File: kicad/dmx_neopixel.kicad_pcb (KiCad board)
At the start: 2 copper layers, 60.5 x 96.3 mm, 32 parts, among them J1 USB_C_Receptacle_USB2.0_16P, J7 Jack-DC

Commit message: feat: v0.2の基板を作成
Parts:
- removed the G*** at (148.1, 123.4)
- removed XH: Conn_01x03_Pin, Connector_JST:JST_XH_B3B-XH-A_1x03_P2.50mm_Vertical
- added ?: http://LDDG.ME/VLLD2N, QRCODE, B.Cu at (152.9, 117.3)
- added MODE: SW_Push, Button_Switch_SMD:SW_SPST_PTS810, B.Cu at (154.2, 56.6)
- added NEOPIXEL OUT: Conn_01x02_Pin, Connector_JST:JST_XH_B2B-XH-A_1x02_P2.50mm_Vertical, F.Cu at (140.0, 54.9)
- moved SW1 24.0 mm to (158.0, 61.5), turned to 180 degrees
- renumbered SS2040FL to D2, MF-R050 to RF-R050, TERMINATE to SW1, ESP32-S3-WROOM-1 to U1
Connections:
- 10k pad 2: LED_DIN -> LED_DATA
- BSS138 pad 2: LED_DIN -> LED_DATA
- SW1 pad 1: DMX_D- -> SW_1
- SW1 pad 10: SW_10 -> DMX_D-
- SW1 pad 11: GND -> Net-(R5-Pad1)
- SW1 pad 20: Net-(R5-Pad1) -> GND
- U1 pad 12: SW_8 -> unconnected-(U1-IO8-Pad12)
- U1 pad 15: SW_3 -> unconnected-(U1-IO3-Pad15)
- U1 pad 17: SW_9 -> SW_6
- U1 pad 18: SW_10 -> SW_7
- U1 pad 19: unconnected-(U1-IO11-Pad19) -> SW_8
- U1 pad 20: unconnected-(U1-IO12-Pad20) -> SW_9
- U1 pad 21: unconnected-(U1-IO13-Pad21) -> LED_DATA
- U1 pad 22: unconnected-(U1-IO14-Pad22) -> SW_MODE
- U1 pad 31: unconnected-(U1-IO38-Pad31) -> SW_5
- U1 pad 32: unconnected-(U1-IO39-Pad32) -> SW_4
- U1 pad 33: unconnected-(U1-IO40-Pad33) -> SW_3
- U1 pad 34: unconnected-(U1-IO41-Pad34) -> SW_2
- U1 pad 35: unconnected-(U1-IO42-Pad35) -> SW_1
- U1 pad 38: SW_2 -> unconnected-(U1-IO2-Pad38)
- U1 pad 39: LED_DIN -> unconnected-(U1-IO1-Pad39)
- U1 pad 4: SW_4 -> unconnected-(U1-IO4-Pad4)
- U1 pad 5: SW_5 -> unconnected-(U1-IO5-Pad5)
- U1 pad 6: SW_6 -> unconnected-(U1-IO6-Pad6)
- U1 pad 7: SW_7 -> unconnected-(U1-IO7-Pad7)
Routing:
- net LED_DATA: track 0.00 -> 55.0 mm
- net SW_MODE: track 0.00 -> 49.3 mm, vias 0 -> 1
- net SW_10: track 47.0 -> 0.00 mm, vias 2 -> 0
- net SW_1: track 0.00 -> 33.0 mm
- net LED_DIN: track 28.8 -> 0.00 mm, vias 2 -> 0
- net SW_9: track 45.1 -> 21.2 mm, vias 2 -> 0
- net DMX_D-: track 92.4 -> 72.0 mm
- net SW_2: track 10.2 -> 28.9 mm
- net SW_8: track 44.0 -> 25.3 mm, vias 2 -> 0
- net SW_5: track 36.4 -> 19.7 mm, vias 2 -> 0
- net SW_4: track 36.4 -> 22.8 mm
- net SW_7: track 41.7 -> 29.5 mm, vias 2 -> 0
- net +5V: track 104.8 -> 95.1 mm, vias 2 -> 3
- net Net-(R5-Pad1): track 16.7 -> 24.0 mm, vias 0 -> 1
- net SW_3: track 32.3 -> 25.9 mm, vias 1 -> 0
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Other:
- board text added: "12V IN"
- board text added: "D"
- board text added: "ESP32-S3-WROOM-1"
- board text added: "G"
- board text added: "SS2040FL"
- board text added: "START CH"
- board text added: "TERMINATE"
- board text added: "https://github.com/VirtualLiveLab/dmx_neopixel v0.2"
- board text removed: "1"
- board text removed: "128"
- board text removed: "16"
- board text removed: "2"
- board text removed: "256"
- board text removed: "32"
- board text removed: "4"
- board text removed: "64"
- board text removed: "8"
- board text removed: "https://github.com/laddge/dmx_neopixel v0.1"

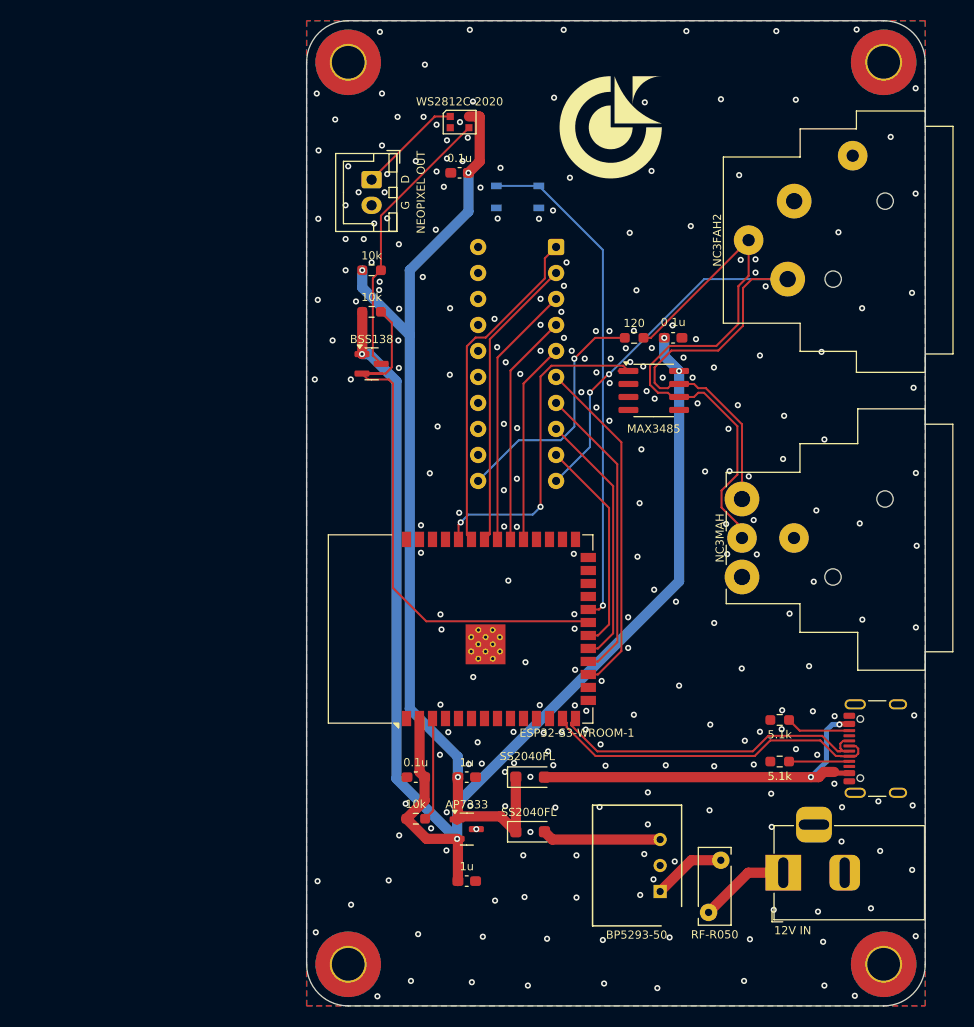
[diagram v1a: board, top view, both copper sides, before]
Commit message: feat: ESP32をC3に変更
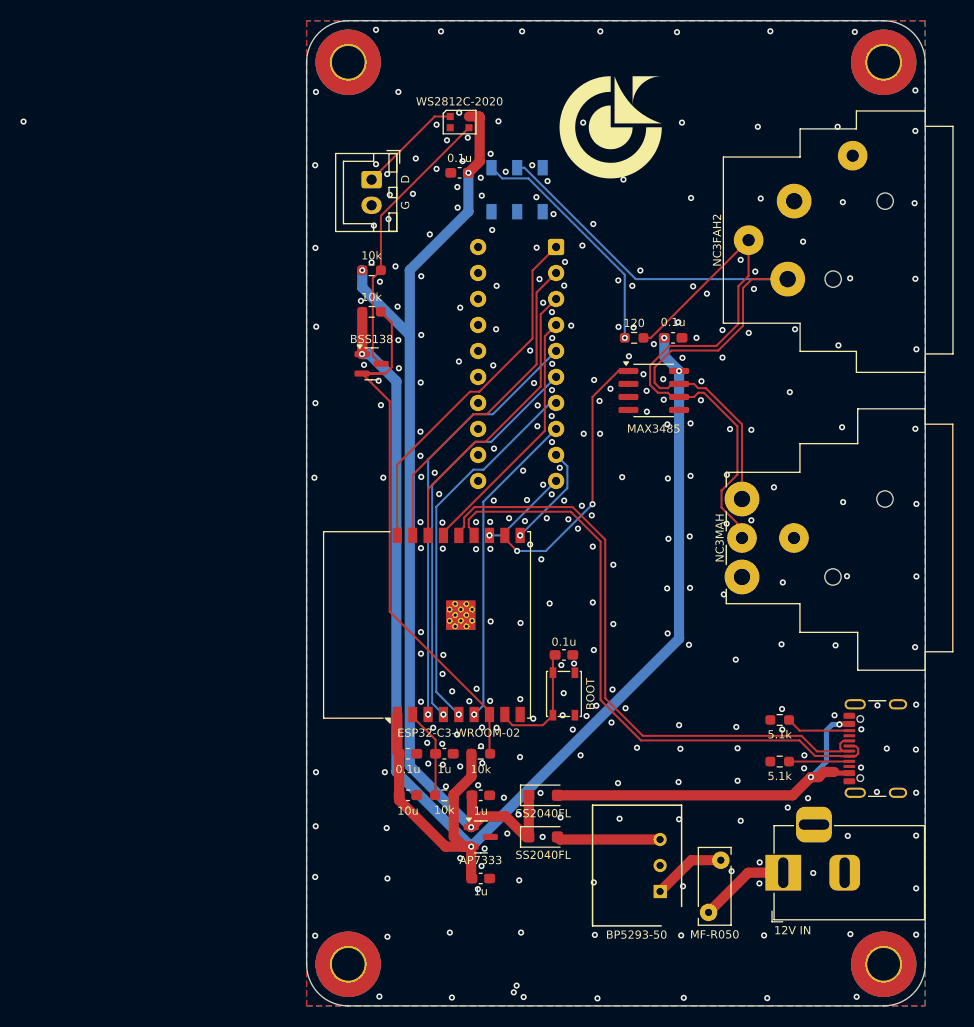
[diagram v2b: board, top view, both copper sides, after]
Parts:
- removed the 0.1u at (144.3, 113.3)
- removed MODE: SW_Push, Button_Switch_SMD:SW_SPST_PTS810
- removed U1: ESP32-S3-WROOM-1, RF_Module:ESP32-S3-WROOM-1
- added 0.1u: 0.1u, Capacitor_SMD:C_0603_1608Metric_Pad1.08x0.95mm_HandSolder, F.Cu at (143.5, 111.0)
- added 0.1u: 0.1u, Capacitor_SMD:C_0603_1608Metric_Pad1.08x0.95mm_HandSolder, F.Cu at (158.8, 101.3)
- added 10k: 10k, Resistor_SMD:R_0603_1608Metric_Pad0.98x0.95mm_HandSolder, F.Cu at (150.6, 111.0)
- added 10u: 10u, Capacitor_SMD:C_0603_1608Metric_Pad1.08x0.95mm_HandSolder, F.Cu at (143.5, 115.1)
- added 1u: 1u, Capacitor_SMD:C_0603_1608Metric_Pad1.08x0.95mm_HandSolder, F.Cu at (147.1, 111.0)
- added BOOT: SW_Push, Button_Switch_SMD:SW_SPST_PTS810, F.Cu at (158.8, 105.2)
- added ESP32-C3-WROOM-02: ESP32-C3-WROOM-02, RF_Module:ESP32-C3-WROOM-02, F.Cu at (148.5, 98.4)
- added SW2: SW_Slide_DPDT, Button_Switch_SMD:SW_DPDT_CK_JS202011JCQN, B.Cu at (154.2, 55.9)
- J5: renamed from NEOPIXEL OUT
- moved 10k 3.61 mm to (147.1, 115.1), turned to 180 degrees
- moved 1u 2.24 mm to (150.6, 115.1)
- moved D2 2.18 mm to (156.7, 115.1)
- moved AP7333 1.57 mm to (150.6, 119.1)
- moved 1u 1.39 mm to (150.6, 123.2)
- moved SS2040FL 1.37 mm to (156.7, 119.1)
- renumbered RF-R050 to MF-R050
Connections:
- net LED_DATA renamed IO8
- MAX3485 pad 1: Net-(U1-RXD0) -> DMX_IN
- SW1 pad 10: DMX_D- -> SW_10
- SW1 pad 11: Net-(R5-Pad1) -> GND
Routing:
- net SW_MODE: track 49.3 -> 0.00 mm, vias 1 -> 0
- net Net-(U1-RXD0): track 33.1 -> 0.00 mm, vias 2 -> 0
- net USB_D+: track 32.8 -> 61.4 mm
- net USB_D-: track 33.5 -> 60.7 mm
- net DMX_IN: track 0.00 -> 26.3 mm, vias 0 -> 2
- net SW_5: track 19.7 -> 41.8 mm, vias 0 -> 1
- net +3.3V: track 135.0 -> 147.3 mm
- net BOOT: track 0.00 -> 11.7 mm
- net SW_9: track 21.2 -> 10.2 mm, vias 0 -> 1
- net SW_10: track 0.00 -> 8.71 mm, vias 0 -> 1
- net SW_7: track 29.5 -> 37.1 mm, vias 0 -> 1
- net SW_8: track 25.3 -> 31.2 mm, vias 0 -> 1
- net SW_6: track 33.6 -> 39.4 mm, vias 0 -> 1
- net SW_2: track 28.9 -> 32.2 mm
- net SW_3: track 25.9 -> 28.9 mm
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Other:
- board text added: "DMX START CHANNEL"
- board text added: "https://github.com/VirtualLiveLab/dmx_neopixel v0.3"
- board text removed: "ESP32-S3-WROOM-1"
- board text removed: "START CH"
- board text removed: "https://github.com/VirtualLiveLab/dmx_neopixel v0.2"

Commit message: feat: v1.0の基板データを追加
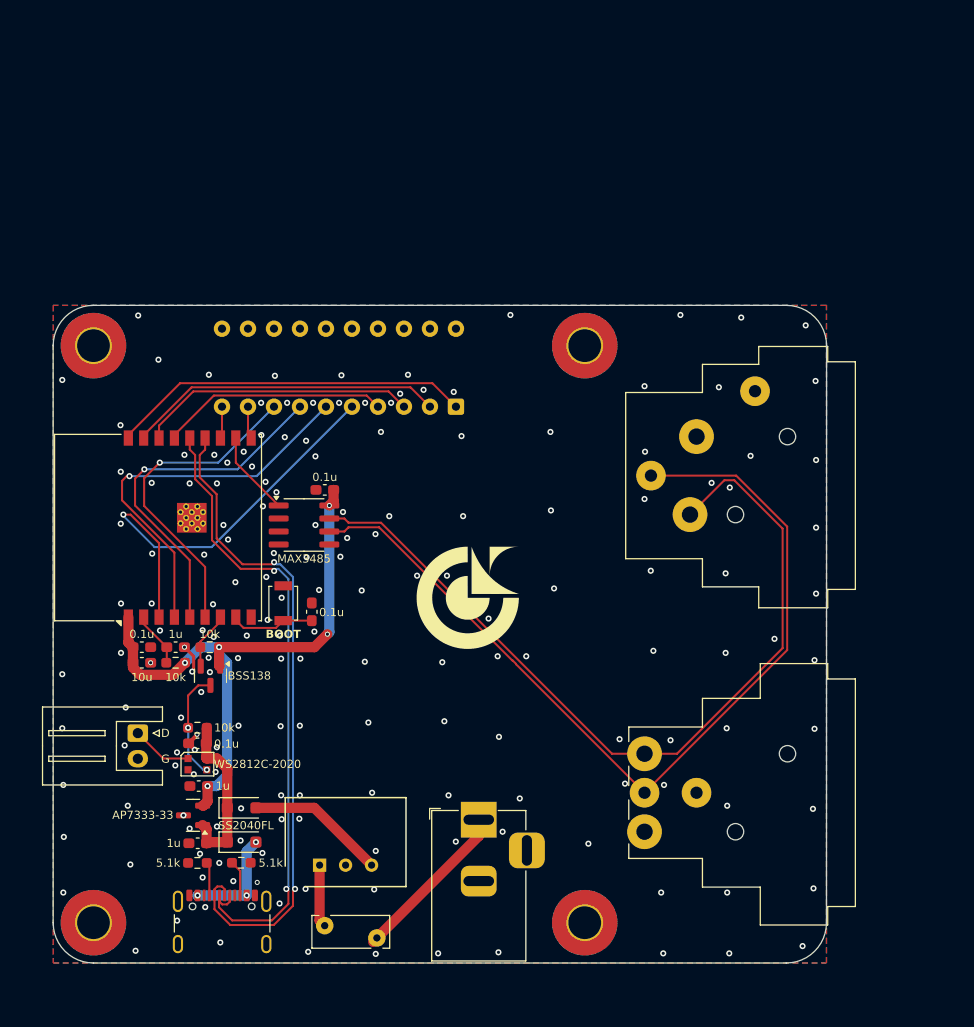
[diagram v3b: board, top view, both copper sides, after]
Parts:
- removed 0.1u (x4): 0.1u, Capacitor_SMD:C_0603_1608Metric_Pad1.08x0.95mm_HandSolder
- removed 10k (x4): 10k, Resistor_SMD:R_0603_1608Metric_Pad0.98x0.95mm_HandSolder
- removed 10u: 10u, Capacitor_SMD:C_0603_1608Metric_Pad1.08x0.95mm_HandSolder
- removed 120: 120, Resistor_SMD:R_0603_1608Metric_Pad0.98x0.95mm_HandSolder
- removed 1u (x3): 1u, Capacitor_SMD:C_0603_1608Metric_Pad1.08x0.95mm_HandSolder
- removed 5.1k (x2): 5.1k, Resistor_SMD:R_0603_1608Metric_Pad0.98x0.95mm_HandSolder
- removed AP7333: AP7333-33SA, Package_TO_SOT_SMD:SOT-23
- removed BOOT: SW_Push, Button_Switch_SMD:SW_SPST_PTS810
- removed BP5293-50: BP5293-50, Package_SIP:SIP3_11.6x8.5mm
- removed BSS138: BSS138, Package_TO_SOT_SMD:SOT-23
- removed ESP32-C3-WROOM-02: ESP32-C3-WROOM-02, RF_Module:ESP32-C3-WROOM-02
- removed J7: Jack-DC, Connector_BarrelJack:BarrelJack_Horizontal
- removed MAX3485: MAX3485, Package_SO:SOIC-8_3.9x4.9mm_P1.27mm
- removed MF-R050: MF-R050, Fuse:Fuse_Bourns_MF-RHT050
- removed NC3FAH2: NC3FAH2, Connector_Audio:Jack_XLR_Neutrik_NC3FAH2_Horizontal
- removed NC3MAH: NC3MAH, Connector_Audio:Jack_XLR_Neutrik_NC3MAH_Horizontal
- removed SS2040FL: SS2040FL, Diode_SMD:D_SOD-123F
- removed WS2812C-2020: WS2812C-2020, LED_SMD:LED_WS2812B-2020_PLCC4_2.0x2.0mm
- added C1: 0.1u, Capacitor_SMD:C_0603_1608Metric_Pad1.08x0.95mm_HandSolder, F.Cu at (134.1, 97.1)
- added C2: 0.1u, Capacitor_SMD:C_0603_1608Metric_Pad1.08x0.95mm_HandSolder, F.Cu at (122.9, 110.0)
- added C3: 1u, Capacitor_SMD:C_0603_1608Metric_Pad1.08x0.95mm_HandSolder, F.Cu at (123.0, 119.7)
- added C4: 10u, Capacitor_SMD:C_0603_1608Metric_Pad1.08x0.95mm_HandSolder, F.Cu at (117.5, 102.1)
- added C5: 0.1u, Capacitor_SMD:C_0603_1608Metric_Pad1.08x0.95mm_HandSolder, F.Cu at (117.5, 100.6)
- added C6: 1u, Capacitor_SMD:C_0603_1608Metric_Pad1.08x0.95mm_HandSolder, F.Cu at (123.1, 114.2)
- added C7: 1u, Capacitor_SMD:C_0603_1608Metric_Pad1.08x0.95mm_HandSolder, F.Cu at (120.8, 100.6)
- added C8: 0.1u, Capacitor_SMD:C_0603_1608Metric_Pad1.08x0.95mm_HandSolder, F.Cu at (135.4, 85.2)
- added D1: SS2040FL, Diode_SMD:D_SOD-123F, F.Cu at (127.3, 119.6)
- added D3: WS2812C-2020, LED_SMD:LED_WS2812B-2020_PLCC4_2.0x2.0mm, F.Cu at (122.9, 112.0)
- added F1: MF-R050, Fuse:Fuse_Bourns_MF-RHT050, F.Cu at (140.5, 129.0)
- added J2: USB_C_Receptacle_USB2.0_16P, Connector_USB:USB_C_Receptacle_GCT_USB4105-xx-A_16P_TopMnt_Horizontal, F.Cu at (125.3, 128.5)
- added J3: Conn_01x02_Pin, Connector_JST:JST_XH_S2B-XH-A_1x02_P2.50mm_Horizontal, F.Cu at (117.1, 109.0)
- added J4: NC3MAH, Connector_Audio:Jack_XLR_Neutrik_NC3MAH_Horizontal, F.Cu at (166.6, 118.6)
- added Q1: BSS138, Package_TO_SOT_SMD:SOT-23, F.Cu at (124.2, 103.4)
- added R1: 5.1k, Resistor_SMD:R_0603_1608Metric_Pad0.98x0.95mm_HandSolder, F.Cu at (122.9, 121.7)
- added R2: 5.1k, Resistor_SMD:R_0603_1608Metric_Pad0.98x0.95mm_HandSolder, F.Cu at (127.2, 121.7)
- added R3: 10k, Resistor_SMD:R_0603_1608Metric_Pad0.98x0.95mm_HandSolder, F.Cu at (124.1, 100.6)
- added R4: 10k, Resistor_SMD:R_0603_1608Metric_Pad0.98x0.95mm_HandSolder, F.Cu at (122.9, 108.5)
- added R5: 10k, Resistor_SMD:R_0603_1608Metric_Pad0.98x0.95mm_HandSolder, F.Cu at (120.8, 102.1)
- added U1: BP5293-50, Package_SIP:SIP3_11.6x8.5mm, F.Cu at (134.9, 121.9)
- added U2: AP7333-33SA, Package_TO_SOT_SMD:SOT-23, F.Cu at (122.5, 117.0)
- added U3: ESP32-C3-WROOM-02, RF_Module:ESP32-C3-WROOM-02, F.Cu at (122.2, 88.9)
- added U4: MAX3485, Package_SO:SOIC-8_3.9x4.9mm_P1.27mm, F.Cu at (133.3, 88.6)
- J1: value USB_C_Receptacle_USB2.0_16P -> Jack-DC; footprint Connector_USB:USB_C_Receptacle_GCT_USB4105-xx-A_16P_TopMnt_Horizontal -> Connector_BarrelJack:BarrelJack_Horizontal
- J5: value Conn_01x02_Pin -> NC3FAH2; footprint Connector_JST:JST_XH_B2B-XH-A_1x02_P2.50mm_Vertical -> Connector_Audio:Jack_XLR_Neutrik_NC3FAH2_Horizontal
- SW1: value SW_DIP_x10 -> SW_Push; footprint Button_Switch_THT:SW_DIP_SPSTx10_Slide_6.7x26.96mm_W7.62mm_P2.54mm_LowProfile -> Button_Switch_SMD:SW_SPST_B3U-1000P; moved to F.Cu
- SW2: value SW_Slide_DPDT -> SW_DIP_x10; footprint Button_Switch_SMD:SW_DPDT_CK_JS202011JCQN -> Button_Switch_THT:SW_DIP_SPSTx10_Slide_6.7x26.96mm_W7.62mm_P2.54mm_LowProfile
- moved H1 98.1 mm to (112.8, 71.1)
- moved H3 87.2 mm to (160.8, 127.5)
- moved G*** 48.0 mm to (149.4, 95.8)
- moved SW1 43.8 mm to (131.3, 96.3), turned to -90 degrees
- moved J1 40.5 mm to (150.4, 117.4)
- moved J5 40.5 mm to (171.7, 80.0), turned to 0 degrees
- moved H2 40.2 mm to (160.8, 71.1)
- moved D2 29.5 mm to (127.3, 116.3)
- moved H4 25.2 mm to (112.8, 127.5)
- moved SW2 22.0 mm to (148.2, 77.1), turned to 90 degrees
- moved ? 18.1 mm to (162.4, 101.9)
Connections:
- J5 pad 1: Net-(D3-DOUT) -> GND
- J5 pad 2: GND -> DMX_D-
- SW1 pad 1: SW_1 -> GND
- SW1 pad 2: SW_2 -> BOOT
- SW2 pad 1: unconnected-(SW2-A-Pad1) -> SW_1
- SW2 pad 2: DMX_D- -> SW_2
- SW2 pad 3: Net-(R5-Pad1) -> SW_3
- SW2 pad 4: unconnected-(SW2-A-Pad4) -> SW_4
- SW2 pad 5: unconnected-(SW2-B-Pad5) -> SW_5
- SW2 pad 6: unconnected-(SW2-C-Pad6) -> SW_6
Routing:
- net +3.3V: track 147.3 -> 59.6 mm, vias 4 -> 5
- net +5V: track 98.1 -> 16.6 mm, vias 3 -> 0
- net IO8: track 53.4 -> 0.00 mm
- net DMX_D+: track 58.0 -> 88.9 mm
- net Net-(D2-A): track 37.2 -> 13.6 mm, vias 2 -> 0
- net Net-(R5-Pad1): track 23.5 -> 0.00 mm, vias 1 -> 0
- net DMX_IN: track 26.3 -> 8.33 mm, vias 2 -> 0
- net Net-(D3-DIN): track 27.3 -> 10.8 mm, vias 0 -> 2
- net DMX_D-: track 69.0 -> 82.2 mm
- net Net-(U5-EN): track 8.84 -> 0.00 mm
- net +12V: track 8.91 -> 16.2 mm
- net Net-(U4-Vin): track 7.20 -> 0.00 mm
- net SW_9: track 10.2 -> 3.18 mm, vias 1 -> 0
- net Net-(J1-CC2): track 6.32 -> 0.00 mm
- net Net-(U1-Vin): track 0.00 -> 6.12 mm
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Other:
- board size 60.5 x 96.3 mm -> 75.6 x 64.3 mm
- board text added: "0.1u"
- board text added: "1"
- board text added: "10"
- board text added: "10k"
- board text added: "10u"
- board text added: "1u"
- board text added: "5.1k"
- board text added: "AP7333-33"
- board text added: "BOOT"
- board text added: "BSS138"
- board text added: "MAX3485"
- board text added: "Virtual Live Lab 2025 https://github.com/VirtualLiveLab/dmx_neopixel v1.0 | Designed by Laddge"
- board text added: "WS2812C-2020"
- board text removed: "12V IN"
- board text removed: "DMX START CHANNEL"
- board text removed: "Designed by Laddge"
- board text removed: "ON"
- board text removed: "TERMINATE"
- board text removed: "Virtual Live Lab 2025"
- board text removed: "https://github.com/VirtualLiveLab/dmx_neopixel v0.3"

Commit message: feat: 基板データ更新
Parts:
- SW1: footprint Button_Switch_SMD:SW_SPST_B3U-1000P -> Button_Switch_SMD:SW_SPST_PTS810
- moved SW1 0.22 mm to (131.5, 96.4), turned to 90 degrees
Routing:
- net BOOT: track 8.33 -> 13.5 mm
- net GND: vias 175 -> 174
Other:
- board text added: "Virtual Live Lab 2025 https://github.com/VirtualLiveLab/dmx_neopixel v1.1 | Designed by Laddge"
- board text removed: "Virtual Live Lab 2025 https://github.com/VirtualLiveLab/dmx_neopixel v1.0 | Designed by Laddge"
